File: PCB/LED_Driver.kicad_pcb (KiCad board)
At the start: 2 copper layers, 61 x 77.8 mm, 8 parts, among them J1 Conn_Coaxial_Power, J4 Conn_01x04_Male, J5 Screw_Terminal_01x05, Q1 IRLB8721PBF, Q2 IRLB8721PBF, Q3 IRLB8721PBF, Q4 IRLB8721PBF, U1 ESP32_DevKit_V1_DOIT

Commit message: minor updates
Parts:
- added REF**: MountingHole_2.2mm_M2, MountingHole:MountingHole_2.2mm_M2, F.Cu at (164.8, 125.6)
- added REF**: MountingHole_2.2mm_M2, MountingHole:MountingHole_2.2mm_M2, F.Cu at (128.2, 58.5)
- added REF**: MountingHole_2.2mm_M2, MountingHole:MountingHole_2.2mm_M2, F.Cu at (164.8, 58.5)
- added REF**: MountingHole_2.2mm_M2, MountingHole:MountingHole_2.2mm_M2, F.Cu at (135.4, 71.7)
- added REF**: MountingHole_2.2mm_M2, MountingHole:MountingHole_2.2mm_M2, F.Cu at (135.4, 119.2)
- added REF**: MountingHole_2.2mm_M2, MountingHole:MountingHole_2.2mm_M2, F.Cu at (112.0, 71.7)
- added REF**: MountingHole_2.2mm_M2, MountingHole:MountingHole_2.2mm_M2, F.Cu at (112.0, 119.2)
- added REF**: MountingHole_2.2mm_M2, MountingHole:MountingHole_2.2mm_M2, F.Cu at (112.0, 125.6)
- renumbered J5 to locked
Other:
- board text added: "D"
- board text added: "Max Current Per Channel: 4A"
- board text added: "S"

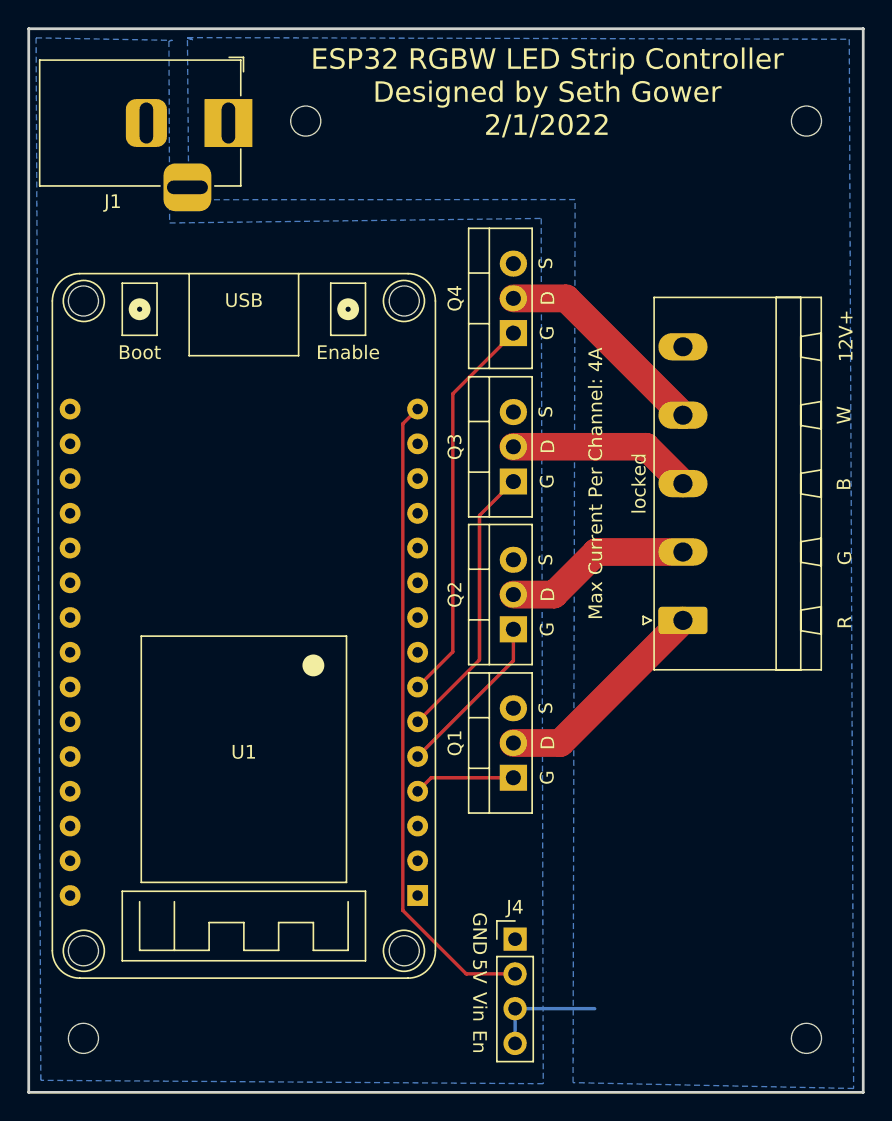
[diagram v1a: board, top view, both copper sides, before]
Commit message: Updates the connections to the ESP32. The original pins were input only pins, according to esphome
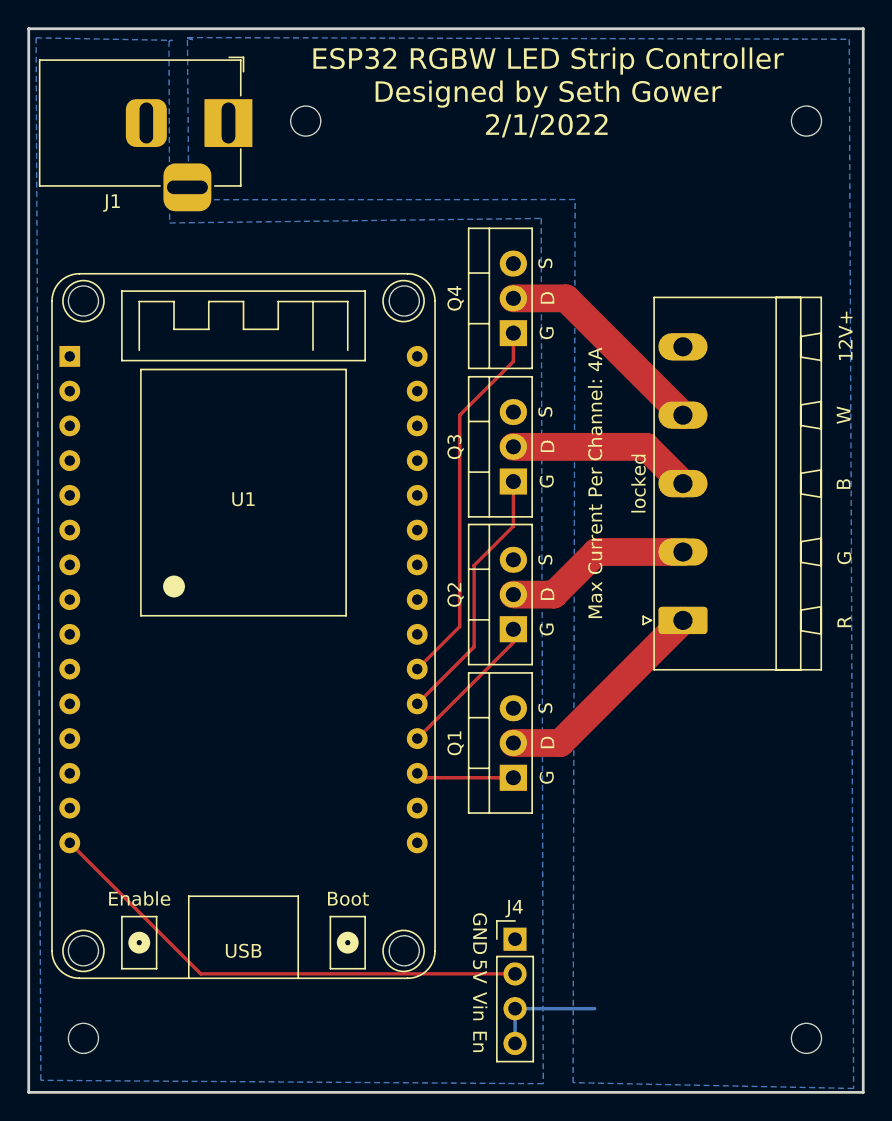
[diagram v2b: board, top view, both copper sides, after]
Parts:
- moved U1 39.4 mm to (123.7, 75.8), turned to 0 degrees
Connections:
- U1 pad 18: unconnected-(U1-Pad18) -> /PWM_R
- U1 pad 19: unconnected-(U1-Pad19) -> /PWM_G
- U1 pad 20: unconnected-(U1-Pad20) -> /PWM_B
- U1 pad 21: unconnected-(U1-Pad21) -> /PWM_W
- U1 pad 4: /PWM_R -> unconnected-(U1-Pad4)
- U1 pad 5: /PWM_G -> unconnected-(U1-Pad5)
- U1 pad 6: /PWM_B -> unconnected-(U1-Pad6)
- U1 pad 7: /PWM_W -> unconnected-(U1-Pad7)
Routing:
- net +5V: track 47.2 -> 36.5 mm
- net /PWM_G: track 12.2 -> 10.9 mm
- net /PWM_W: track 28.8 -> 27.5 mm
- net /PWM_B: track 20.5 -> 19.2 mm

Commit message: Makes board smaller using proper terminal blocks
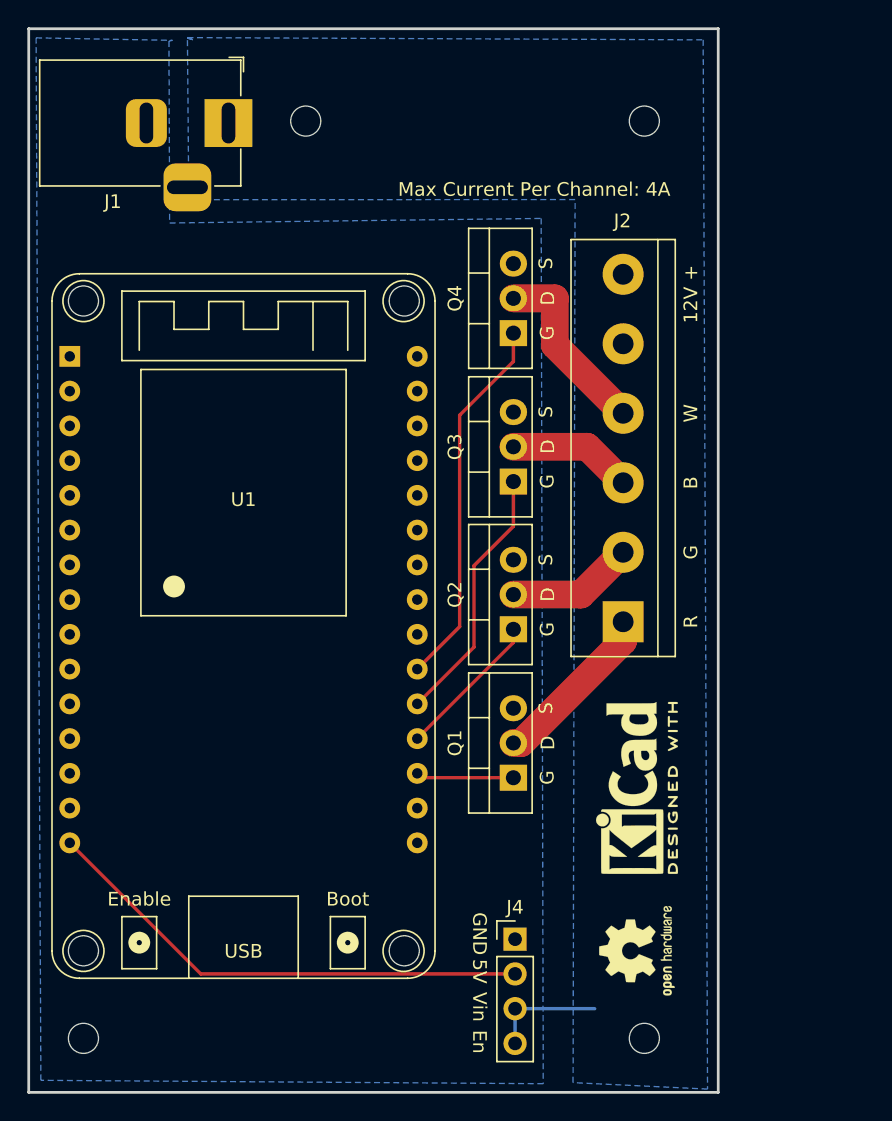
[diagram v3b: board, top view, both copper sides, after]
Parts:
- removed locked: Screw_Terminal_01x05, Connector_Phoenix_MSTB:PhoenixContact_MSTBA_2,5_5-G_1x05_P5.00mm_Horizontal
- added J2: Screw_Terminal_01x06, TerminalBlock:TerminalBlock_bornier-6_P5.08mm, F.Cu at (151.4, 95.2)
- added REF**: KiCad-Logo2_5mm_SilkScreen, Symbol:KiCad-Logo2_5mm_SilkScreen, F.Cu at (152.4, 107.3)
- added REF**: OSHW-Logo2_7.3x6mm_SilkScreen, Symbol:OSHW-Logo2_7.3x6mm_SilkScreen, F.Cu at (152.4, 119.2)
- moved REF** 11.9 mm to (152.9, 125.6)
- moved REF** 11.9 mm to (152.9, 58.5)
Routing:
- net LED_B: track 13.5 -> 9.11 mm
- net LED_G: track 13.7 -> 9.30 mm
- net LED_R: track 16.1 -> 12.5 mm
- net LED_W: track 15.9 -> 13.5 mm
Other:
- board size 61 x 77.8 mm -> 50.4 x 77.8 mm
- board text added: "12V +"
- board text added: "ESP32 RGBW LED Strip Controller Designed by Seth Gower https://github.com/sethgower/leddriverboard"
- board text removed: "12V+"
- board text removed: "ESP32 RGBW LED Strip Controller Designed by Seth Gower 2/1/2022"

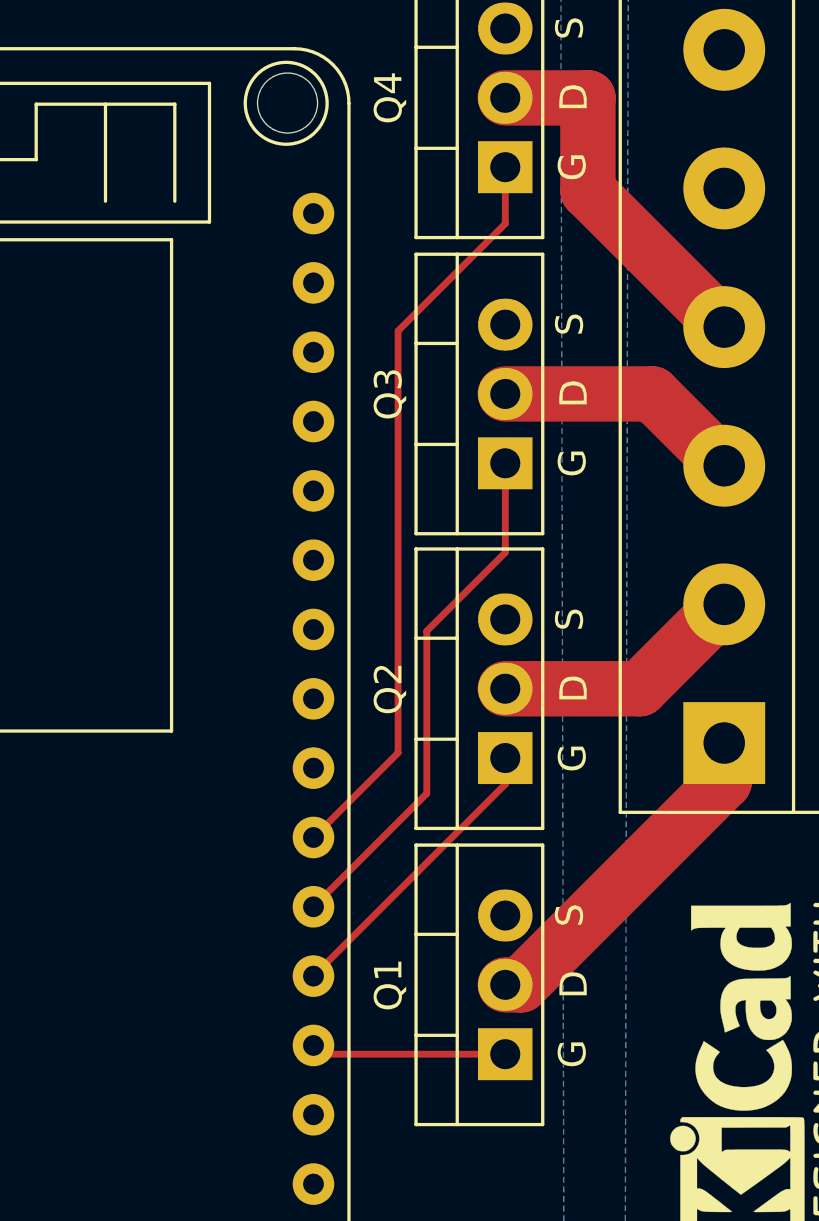
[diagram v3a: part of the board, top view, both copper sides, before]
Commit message: Updates pins that are driving gates of transistors. 3 of the original ones were strapping pins on the esp32
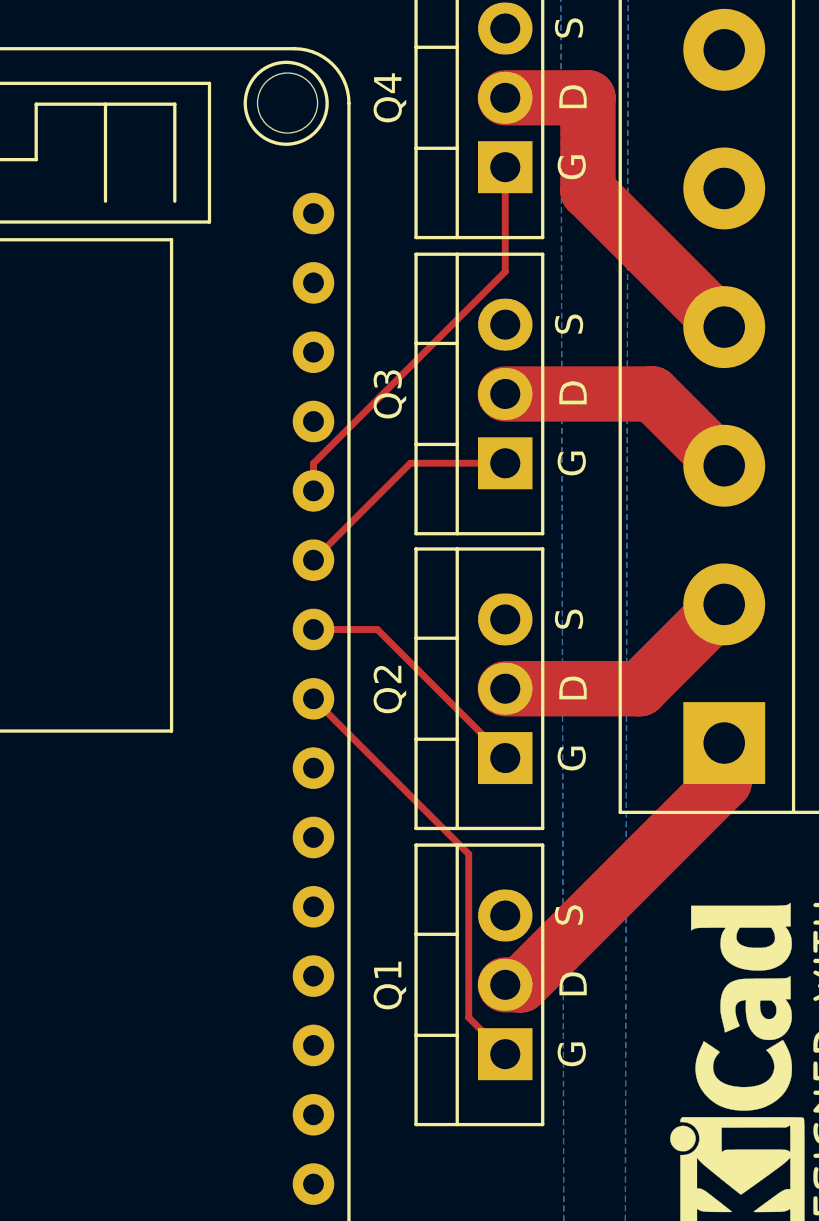
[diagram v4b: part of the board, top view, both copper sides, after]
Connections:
- U1 pad 18: /PWM_R -> unconnected-(U1-Pad18)
- U1 pad 19: /PWM_G -> unconnected-(U1-Pad19)
- U1 pad 20: /PWM_B -> unconnected-(U1-Pad20)
- U1 pad 21: /PWM_W -> unconnected-(U1-Pad21)
- U1 pad 23: unconnected-(U1-Pad23) -> /PWM_R
- U1 pad 24: unconnected-(U1-Pad24) -> /PWM_G
- U1 pad 25: unconnected-(U1-Pad25) -> /PWM_B
- U1 pad 26: unconnected-(U1-Pad26) -> /PWM_W
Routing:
- net /PWM_W: track 27.5 -> 14.8 mm
- net /PWM_B: track 19.2 -> 8.50 mm
- net /PWM_R: track 7.16 -> 15.9 mm
- net /PWM_G: track 10.9 -> 8.99 mm
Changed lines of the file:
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@@
   (net 25 "unconnected-(U1-Pad7)")
   (net 26 "unconnected-(U1-Pad22)")
-  (net 27 "unconnected-(U1-Pad23)")
-  (net 28 "unconnected-(U1-Pad24)")
-  (net 29 "unconnected-(U1-Pad25)")
-  (net 30 "unconnected-(U1-Pad26)")
+  (net 27 "unconnected-(U1-Pad18)")
+  (net 28 "unconnected-(U1-Pad19)")
+  (net 29 "unconnected-(U1-Pad20)")
+  (net 30 "unconnected-(U1-Pad21)")
   (net 31 "unconnected-(U1-Pad27)")
   (net 32 "unconnected-(U1-Pad28)")
@@
       (net 2 "GND") (pinfunction "GND") (pintype "power_in"))
     (pad "18" thru_hole circle locked (at 12.7 30.48) (size 1.524 1.524) (drill 0.762) (layers *.Cu *.Mask)
-      (net 8 "/PWM_R") (pinfunction "IO15") (pintype "bidirectional"))
+      (net 27 "unconnected-(U1-Pad18)") (pinfunction "IO15") (pintype "bidirectional+no_connect"))
     (pad "19" thru_hole circle locked (at 12.7 27.94) (size 1.524 1.524) (drill 0.762) (layers *.Cu *.Mask)
-      (net 9 "/PWM_G") (pinfunction "IO2") (pintype "bidirectional"))
+      (net 28 "unconnected-(U1-Pad19)") (pinfunction "IO2") (pintype "bidirectional+no_connect"))
     (pad "20" thru_hole circle locked (at 12.7 25.4) (size 1.524 1.524) (drill 0.762) (layers *.Cu *.Mask)
-      (net 10 "/PWM_B") (pinfunction "IO4") (pintype "bidirectional"))
+      (net 29 "unconnected-(U1-Pad20)") (pinfunction "IO4") (pintype "bidirectional+no_connect"))
     (pad "21" thru_hole circle locked (at 12.7 22.86) (size 1.524 1.524) (drill 0.762) (layers *.Cu *.Mask)
-      (net 11 "/PWM_W") (pinfunction "IO16") (pintype "bidirectional"))
+      (net 30 "unconnected-(U1-Pad21)") (pinfunction "IO16") (pintype "bidirectional+no_connect"))
     (pad "22" thru_hole circle locked (at 12.7 20.32) (size 1.524 1.524) (drill 0.762) (layers *.Cu *.Mask)
       (net 26 "unconnected-(U1-Pad22)") (pinfunction "IO17") (pintype "bidirectional+no_connect"))
     (pad "23" thru_hole circle locked (at 12.7 17.78) (size 1.524 1.524) (drill 0.762) (layers *.Cu *.Mask)
-      (net 27 "unconnected-(U1-Pad23)") (pinfunction "IO5") (pintype "bidirectional+no_connect"))
+      (net 8 "/PWM_R") (pinfunction "IO5") (pintype "bidirectional"))
     (pad "24" thru_hole circle locked (at 12.7 15.24) (size 1.524 1.524) (drill 0.762) (layers *.Cu *.Mask)
-      (net 28 "unconnected-(U1-Pad24)") (pinfunction "IO18") (pintype "bidirectional+no_connect"))
+      (net 9 "/PWM_G") (pinfunction "IO18") (pintype "bidirectional"))
     (pad "25" thru_hole circle locked (at 12.7 12.7) (size 1.524 1.524) (drill 0.762) (layers *.Cu *.Mask)
-      (net 29 "unconnected-(U1-Pad25)") (pinfunction "IO19") (pintype "bidirectional+no_connect"))
+      (net 10 "/PWM_B") (pinfunction "IO19") (pintype "bidirectional"))
     (pad "26" thru_hole circle locked (at 12.7 10.16) (size 1.524 1.524) (drill 0.762) (layers *.Cu *.Mask)
-      (net 30 "unconnected-(U1-Pad26)") (pinfunction "IO21") (pintype "bidirectional+no_connect"))
+      (net 11 "/PWM_W") (pinfunction "IO21") (pintype "bidirectional"))
     (pad "27" thru_hole circle locked (at 12.7 7.62) (size 1.524 1.524) (drill 0.762) (layers *.Cu *.Mask)
       (net 31 "unconnected-(U1-Pad27)") (pinfunction "RXD0/IO3") (pintype "bidirectional+no_connect"))
@@
   )
   (dimension (type aligned) (layer "User.1")
-    (pts (xy 105.8 129.55) (xy 105.8 51.8))
-    (height -2.15)
-    (gr_text "3.0610 in" (at 102.5 90.675 90) (layer "User.1")
-      (effects (font (size 1 1) (thickness 0.15)))
-    )
-    (format (units 0) (units_format 1) (precision 4))
-    (style (thickness 0.15) (arrow_length 1.27) (text_position_mode 0) (extension_height 0.58642) (extension_offset 0.5) keep_text_aligned)
-  )
-  (dimension (type aligned) (layer "User.1")
-    (pts (xy 107.95 51.8) (xy 158.35 51.8))
-    (height -4.15)
-    (gr_text "1.9843 in" (at 133.15 46.5) (layer "User.1")
-      (effects (font (size 1 1) (thickness 0.15)))
-    )
-    (format (units 0) (units_format 1) (precision 4))
-    (style (thickness 0.15) (arrow_length 1.27) (text_position_mode 0) (extension_height 0.58642) (extension_offset 0.5) keep_text_aligned)
-  )
-  (dimension (type aligned) (layer "User.1")
     (pts (xy 107.95 51.8) (xy 158.35 51.8))
     (height -1.45)
@@
   (segment (start 146.4075 74.9175) (end 151.4 79.91) (width 2.03) (layer "F.Cu") (net 7))
   (segment (start 146.4075 71.51) (end 146.4075 74.9175) (width 2.03) (layer "F.Cu") (net 7))
-  (segment (start 136.67 106.55) (end 136.35 106.23) (width 0.25) (layer "F.Cu") (net 8))
-  (segment (start 143.3775 106.55) (end 136.67 106.55) (width 0.25) (layer "F.Cu") (net 8))
-  (segment (start 143.3775 95.7) (end 143.3775 96.6625) (width 0.25) (layer "F.Cu") (net 9))
-  (segment (start 143.3775 96.6625) (end 136.35 103.69) (width 0.25) (layer "F.Cu") (net 9))
-  (segment (start 140.5 91.05) (end 140.5 97) (width 0.25) (layer "F.Cu") (net 10))
-  (segment (start 143.3775 84.9) (end 143.3775 88.1725) (width 0.25) (layer "F.Cu") (net 10))
-  (segment (start 140.5 97) (end 136.35 101.15) (width 0.25) (layer "F.Cu") (net 10))
-  (segment (start 143.3775 88.1725) (end 140.5 91.05) (width 0.25) (layer "F.Cu") (net 10))
-  (segment (start 139.45 95.51) (end 136.35 98.61) (width 0.25) (layer "F.Cu") (net 11))
-  (segment (start 143.3775 76.1225) (end 139.45 80.05) (width 0.25) (layer "F.Cu") (net 11))
-  (segment (start 139.45 80.05) (end 139.45 95.51) (width 0.25) (layer "F.Cu") (net 11))
-  (segment (start 143.3775 74.05) (end 143.3775 76.1225) (width 0.25) (layer "F.Cu") (net 11))
+  (segment (start 142.03798 99.21798) (end 136.35 93.53) (width 0.25) (layer "F.Cu") (net 8))
+  (segment (start 143.3775 106.55) (end 142.03798 105.21048) (width 0.25) (layer "F.Cu") (net 8))
+  (segment (start 142.03798 105.21048) (end 142.03798 99.21798) (width 0.25) (layer "F.Cu") (net 8))
+  (segment (start 143.3775 95.6775) (end 138.69 90.99) (width 0.25) (layer "F.Cu") (net 9))
+  (segment (start 138.69 90.99) (end 136.35 90.99) (width 0.25) (layer "F.Cu") (net 9))
+  (segment (start 143.3775 95.7) (end 143.3775 95.6775) (width 0.25) (layer "F.Cu") (net 9))
+  (segment (start 139.9 84.9) (end 136.35 88.45) (width 0.25) (layer "F.Cu") (net 10))
+  (segment (start 143.3775 84.9) (end 139.9 84.9) (width 0.25) (layer "F.Cu") (net 10))
+  (segment (start 143.3775 74.05) (end 143.3775 77.87906) (width 0.25) (layer "F.Cu") (net 11))
+  (segment (start 143.3775 77.87906) (end 136.35 84.90656) (width 0.25) (layer "F.Cu") (net 11))
+  (segment (start 136.35 84.90656) (end 136.35 85.91) (width 0.25) (layer "F.Cu") (net 11))
   (zone (net 1) (net_name "+12V") (layer "B.Cu") (hatch edge 0.508)
     (connect_pads yes (clearance 0.508))
